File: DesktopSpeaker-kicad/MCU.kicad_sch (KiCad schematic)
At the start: 7 parts, among them J6 SWD, J7 SWD_TC2030, U3 STM32G031K8T6

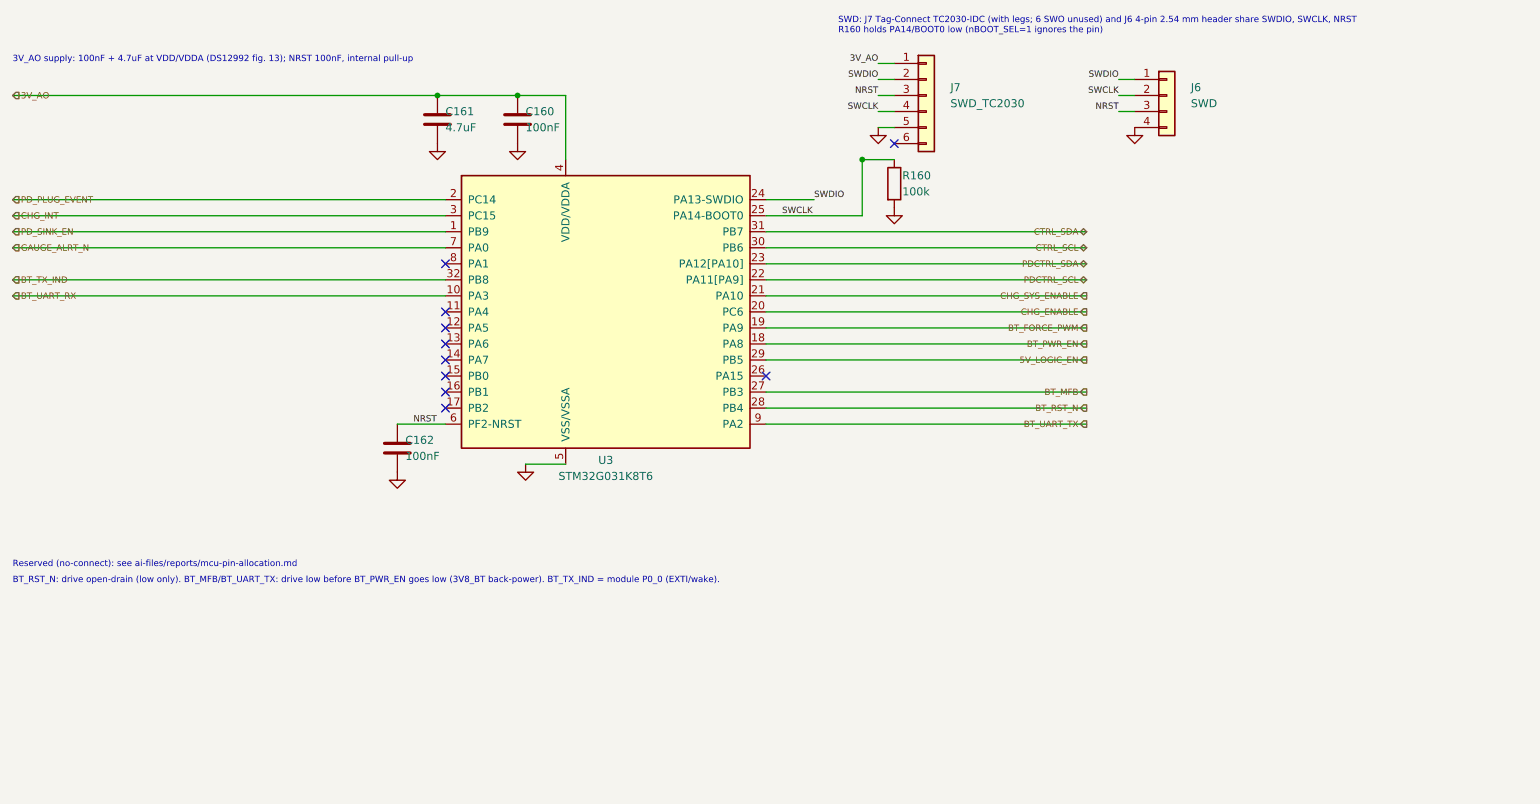
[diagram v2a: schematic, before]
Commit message: Swap MCU to STM32G071RBT6; full audio-chain pin allocation and QON sense
Co-Authored-By: Claude Sonnet 5.5 <noreply@anthropic.com>
Claude-Session: https://claude.ai/code/session_01N5RHheWSjDFDPbKVD5YVeJ
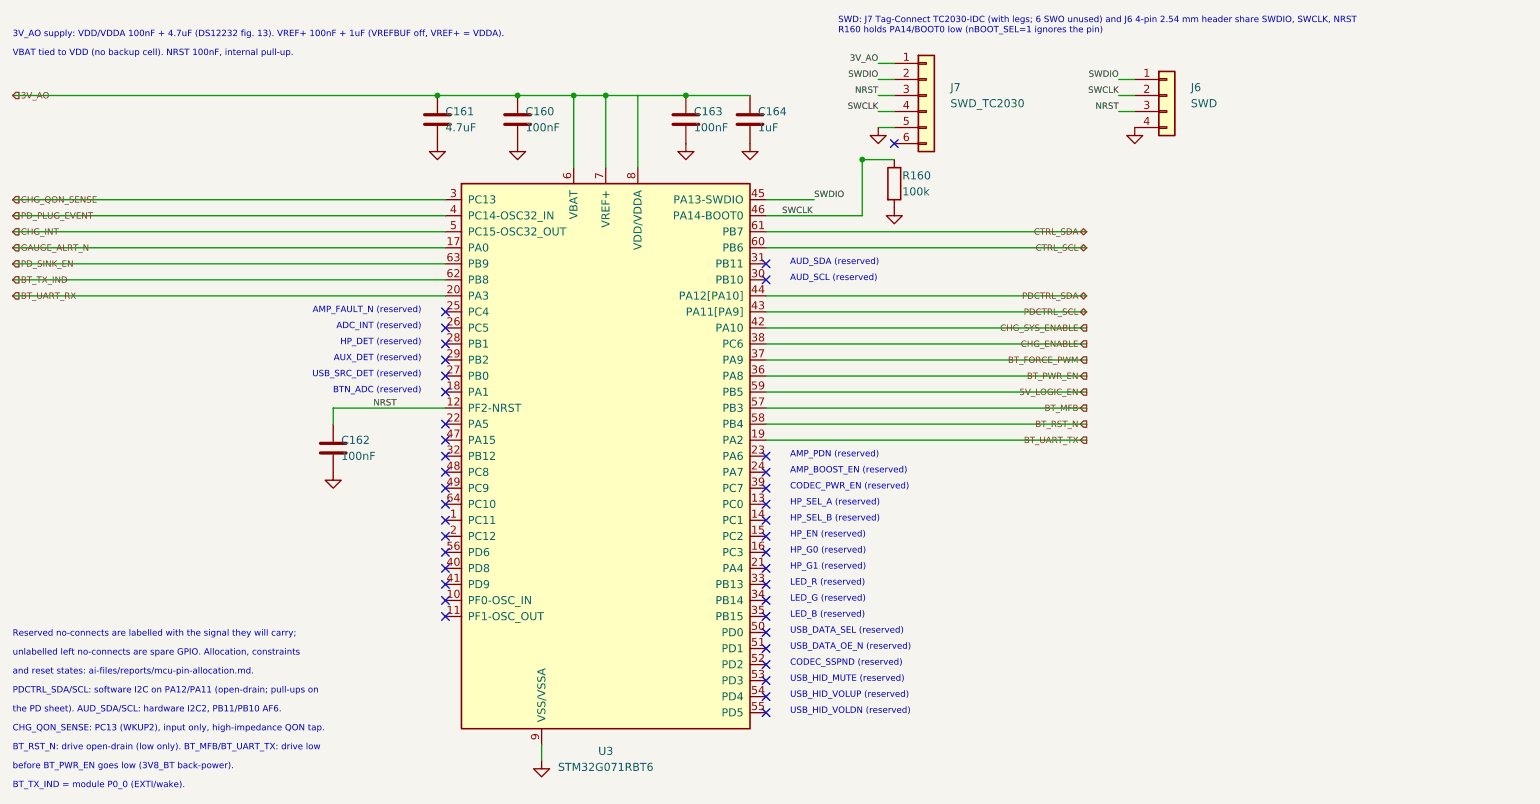
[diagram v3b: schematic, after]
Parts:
- added C163: 100nF, DesktopSpeaker:PD_C_0603, symbol PD_C:PD_C
- added C164: 1uF, DesktopSpeaker:PD_C_0603, symbol PD_C:PD_C
- U3: value STM32G031K8T6 -> STM32G071RBT6; footprint DesktopSpeaker:STM32G031K8T6 -> DesktopSpeaker:STM32G071RBT6; symbol STM32G031K8T6:STM32G031K8T6 -> STM32G071RBT6:STM32G071RBT6; LCSC Part C432203 -> C432213; MPN STM32G031K8T6 -> STM32G071RBT6
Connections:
- net 3V_AO: now also U3.6 (VBAT), U3.7 (VREF+), U3.8 (VDD/VDDA), C163.1, C164.1; no longer U3.4 (VDD/VDDA)
- net 5V_LOGIC_EN: now also U3.59 (PB5); no longer U3.29 (PB5)
- net BT_FORCE_PWM: now also U3.37 (PA9); no longer U3.19 (PA9)
- net BT_MFB: now also U3.57 (PB3); no longer U3.27 (PB3)
- net BT_PWR_EN: now also U3.36 (PA8); no longer U3.18 (PA8)
- net BT_RST_N: now also U3.58 (PB4); no longer U3.28 (PB4)
- net BT_TX_IND: now also U3.62 (PB8); no longer U3.32 (PB8)
- net BT_UART_RX: now also U3.20 (PA3); no longer U3.10 (PA3)
- net BT_UART_TX: now also U3.19 (PA2); no longer U3.9 (PA2)
- net CHG_ENABLE: now also U3.38 (PC6); no longer U3.20 (PC6)
- net CHG_INT: now also U3.5 (PC15-OSC32_OUT); no longer U3.3 (PC15)
- net CHG_SYS_ENABLE: now also U3.42 (PA10); no longer U3.21 (PA10)
- net CTRL_SCL: now also U3.60 (PB6); no longer U3.30 (PB6)
- net CTRL_SDA: now also U3.61 (PB7); no longer U3.31 (PB7)
- net GAUGE_ALRT_N: now also U3.17 (PA0); no longer U3.7 (PA0)
- net GND: now also U3.9 (VSS/VSSA), C163.2, C164.2; no longer U3.5 (VSS/VSSA)
- net NRST: now also U3.12 (PF2-NRST); no longer U3.6 (PF2-NRST)
- net PDCTRL_SCL: now also U3.43 (PA11[PA9]); no longer U3.22 (PA11[PA9])
- net PDCTRL_SDA: now also U3.44 (PA12[PA10]); no longer U3.23 (PA12[PA10])
- net PD_PLUG_EVENT: now also U3.4 (PC14-OSC32_IN); no longer U3.2 (PC14)
- net PD_SINK_EN: now also U3.63 (PB9); no longer U3.1 (PB9)
- net SWCLK: now also U3.46 (PA14-BOOT0); no longer U3.25 (PA14-BOOT0)
- net SWDIO: now also U3.45 (PA13-SWDIO); no longer U3.24 (PA13-SWDIO)
- new net CHG_QON_SENSE: U3.3 (PC13)
- no-connect marks 10 -> 39
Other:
- note added: "3V_AO supply: VDD/VDDA 100nF + 4.7uF (DS12232 fig. 13). VREF+ 100nF + 1uF (VREFBUF off, VREF+ = VDDA)."
- note added: "ADC_INT (reserved)"
- note added: "AMP_BOOST_EN (reserved)"
- note added: "AMP_FAULT_N (reserved)"
- note added: "AMP_PDN (reserved)"
- note added: "AUD_SCL (reserved)"
- note added: "AUD_SDA (reserved)"
- note added: "AUX_DET (reserved)"
- note added: "BTN_ADC (reserved)"
- note added: "BT_RST_N: drive open-drain (low only). BT_MFB/BT_UART_TX: drive low"
- note added: "BT_TX_IND = module P0_0 (EXTI/wake)."
- note added: "CHG_QON_SENSE: PC13 (WKUP2), input only, high-impedance QON tap."
- note added: "CODEC_PWR_EN (reserved)"
- note added: "CODEC_SSPND (reserved)"
- note added: "HP_DET (reserved)"
- note added: "HP_EN (reserved)"
- note added: "HP_G0 (reserved)"
- note added: "HP_G1 (reserved)"
- note added: "HP_SEL_A (reserved)"
- note added: "HP_SEL_B (reserved)"
- note added: "LED_B (reserved)"
- note added: "LED_G (reserved)"
- note added: "LED_R (reserved)"
- note added: "PDCTRL_SDA/SCL: software I2C on PA12/PA11 (open-drain; pull-ups on"
- note added: "Reserved no-connects are labelled with the signal they will carry;"
- note added: "USB_DATA_OE_N (reserved)"
- note added: "USB_DATA_SEL (reserved)"
- note added: "USB_HID_MUTE (reserved)"
- note added: "USB_HID_VOLDN (reserved)"
- note added: "USB_HID_VOLUP (reserved)"
- note added: "USB_SRC_DET (reserved)"
- note added: "VBAT tied to VDD (no backup cell). NRST 100nF, internal pull-up."
- note added: "and reset states: ai-files/reports/mcu-pin-allocation.md."
- note added: "before BT_PWR_EN goes low (3V8_BT back-power)."
- note added: "the PD sheet). AUD_SDA/SCL: hardware I2C2, PB11/PB10 AF6."
- note added: "unlabelled left no-connects are spare GPIO. Allocation, constraints"
- note removed: "3V_AO supply: 100nF + 4.7uF at VDD/VDDA (DS12992 fig. 13); NRST 100nF, internal pull-up"
- note removed: "BT_RST_N: drive open-drain (low only). BT_MFB/BT_UART_TX: drive low before BT_PWR_EN goes low (3V8_BT back-power). BT_TX_IND = module P0_0 (EXTI/wake)."
- note removed: "Reserved (no-connect): see ai-files/reports/mcu-pin-allocation.md"
- moved on the sheet: C162

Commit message: Capture Source_Select_ADC sheet (PCM1862, 3V3_AUDIO LDO, codec load switch)
Co-Authored-By: Claude Sonnet 5.5 <noreply@anthropic.com>
Claude-Session: https://claude.ai/code/session_01N5RHheWSjDFDPbKVD5YVeJ
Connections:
- net ADC_INT: now reaches U3.26 (PC5)
- net AUD_SCL: now reaches U3.30 (PB10)
- net AUD_SDA: now reaches U3.31 (PB11)
- net CODEC_PWR_EN: now reaches U3.39 (PC7)
- no-connect marks 39 -> 35
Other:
- note removed: "ADC_INT (reserved)"
- note removed: "AUD_SCL (reserved)"
- note removed: "AUD_SDA (reserved)"
- note removed: "CODEC_PWR_EN (reserved)"
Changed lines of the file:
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@@
 (no_connect (at 114.3 100.33))
 (text "AMP_FAULT_N (reserved)" (at 110.49 100.73 0) (effects (font (size 1 1)) (justify right bottom)))
-(no_connect (at 114.3 102.87))
-(text "ADC_INT (reserved)" (at 110.49 103.27 0) (effects (font (size 1 1)) (justify right bottom)))
 (no_connect (at 114.3 105.41))
 (text "HP_DET (reserved)" (at 110.49 105.81 0) (effects (font (size 1 1)) (justify right bottom)))
@@
 (wire (pts (xy 165.1 90.17) (xy 215.9 90.17)) (stroke (width 0) (type default)))
 (hierarchical_label "CTRL_SCL" (shape bidirectional) (at 215.9 90.17 0) (effects (font (size 1.0 1.0)) (justify right bottom)))
-(no_connect (at 165.1 92.71))
-(text "AUD_SDA (reserved)" (at 168.91 93.11 0) (effects (font (size 1 1)) (justify left bottom)))
-(no_connect (at 165.1 95.25))
-(text "AUD_SCL (reserved)" (at 168.91 95.65 0) (effects (font (size 1 1)) (justify left bottom)))
 (wire (pts (xy 165.1 97.79) (xy 215.9 97.79)) (stroke (width 0) (type default)))
 (hierarchical_label "PDCTRL_SDA" (shape bidirectional) (at 215.9 97.79 0) (effects (font (size 1.0 1.0)) (justify right bottom)))
@@
 (no_connect (at 165.1 125.73))
 (text "AMP_BOOST_EN (reserved)" (at 168.91 126.13 0) (effects (font (size 1 1)) (justify left bottom)))
-(no_connect (at 165.1 128.27))
-(text "CODEC_PWR_EN (reserved)" (at 168.91 128.67 0) (effects (font (size 1 1)) (justify left bottom)))
 (no_connect (at 165.1 130.81))
 (text "HP_SEL_A (reserved)" (at 168.91 131.21 0) (effects (font (size 1 1)) (justify left bottom)))
@@
 (text "before BT_PWR_EN goes low (3V8_BT back-power)." (at 45.72 173 0) (effects (font (size 1 1)) (justify left bottom)))
 (text "BT_TX_IND = module P0_0 (EXTI/wake)." (at 45.72 176 0) (effects (font (size 1 1)) (justify left bottom)))
+(wire (pts (xy 165.1 92.71) (xy 215.9 92.71)) (stroke (width 0) (type default)))
+(hierarchical_label "AUD_SDA" (shape bidirectional) (at 215.9 92.71 0) (effects (font (size 1.0 1.0)) (justify right bottom)))
+(wire (pts (xy 165.1 95.25) (xy 215.9 95.25)) (stroke (width 0) (type default)))
+(hierarchical_label "AUD_SCL" (shape bidirectional) (at 215.9 95.25 0) (effects (font (size 1.0 1.0)) (justify right bottom)))
+(wire (pts (xy 165.1 128.27) (xy 215.9 128.27)) (stroke (width 0) (type default)))
+(hierarchical_label "CODEC_PWR_EN" (shape output) (at 215.9 128.27 0) (effects (font (size 1.0 1.0)) (justify right bottom)))
+(wire (pts (xy 45.72 102.87) (xy 114.3 102.87)) (stroke (width 0) (type default)))
+(hierarchical_label "ADC_INT" (shape input) (at 45.72 102.87 0) (effects (font (size 1.0 1.0)) (justify left bottom)))
 )

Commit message: Capture Headphone_Aux sheet (TS5A23157 mux, TPA6132A2, jacks) and wire MCU headphone signals
Co-Authored-By: Claude Sonnet 5.5 <noreply@anthropic.com>
Claude-Session: https://claude.ai/code/session_01N5RHheWSjDFDPbKVD5YVeJ
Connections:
- net HP_SEL_A: now reaches U3.13 (PC0)
- net HP_SEL_B: now reaches U3.14 (PC1)
- net HP_EN: now reaches U3.15 (PC2)
- net HP_G0: now reaches U3.16 (PC3)
- net HP_G1: now reaches U3.21 (PA4)
- net HP_DET: now reaches U3.28 (PB1)
- net AUX_DET: now reaches U3.29 (PB2)
- no-connect marks 35 -> 28
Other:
- note removed: "AUX_DET (reserved)"
- note removed: "HP_DET (reserved)"
- note removed: "HP_EN (reserved)"
- note removed: "HP_G0 (reserved)"
- note removed: "HP_G1 (reserved)"
- note removed: "HP_SEL_A (reserved)"
- note removed: "HP_SEL_B (reserved)"
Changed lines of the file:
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@@
 (no_connect (at 114.3 100.33))
 (text "AMP_FAULT_N (reserved)" (at 110.49 100.73 0) (effects (font (size 1 1)) (justify right bottom)))
-(no_connect (at 114.3 105.41))
-(text "HP_DET (reserved)" (at 110.49 105.81 0) (effects (font (size 1 1)) (justify right bottom)))
-(no_connect (at 114.3 107.95))
-(text "AUX_DET (reserved)" (at 110.49 108.35 0) (effects (font (size 1 1)) (justify right bottom)))
 (no_connect (at 114.3 110.49))
 (text "USB_SRC_DET (reserved)" (at 110.49 110.89 0) (effects (font (size 1 1)) (justify right bottom)))
@@
 (no_connect (at 165.1 125.73))
 (text "AMP_BOOST_EN (reserved)" (at 168.91 126.13 0) (effects (font (size 1 1)) (justify left bottom)))
-(no_connect (at 165.1 130.81))
-(text "HP_SEL_A (reserved)" (at 168.91 131.21 0) (effects (font (size 1 1)) (justify left bottom)))
-(no_connect (at 165.1 133.35))
-(text "HP_SEL_B (reserved)" (at 168.91 133.75 0) (effects (font (size 1 1)) (justify left bottom)))
-(no_connect (at 165.1 135.89))
-(text "HP_EN (reserved)" (at 168.91 136.29 0) (effects (font (size 1 1)) (justify left bottom)))
-(no_connect (at 165.1 138.43))
-(text "HP_G0 (reserved)" (at 168.91 138.83 0) (effects (font (size 1 1)) (justify left bottom)))
-(no_connect (at 165.1 140.97))
-(text "HP_G1 (reserved)" (at 168.91 141.37 0) (effects (font (size 1 1)) (justify left bottom)))
 (no_connect (at 165.1 143.51))
 (text "LED_R (reserved)" (at 168.91 143.91 0) (effects (font (size 1 1)) (justify left bottom)))
@@
 (wire (pts (xy 45.72 102.87) (xy 114.3 102.87)) (stroke (width 0) (type default)))
 (hierarchical_label "ADC_INT" (shape input) (at 45.72 102.87 0) (effects (font (size 1.0 1.0)) (justify left bottom)))
+(wire (pts (xy 165.1 130.81) (xy 215.9 130.81)) (stroke (width 0) (type default)))
+(hierarchical_label "HP_SEL_A" (shape output) (at 215.9 130.81 0) (effects (font (size 1.0 1.0)) (justify right bottom)))
+(wire (pts (xy 165.1 133.35) (xy 215.9 133.35)) (stroke (width 0) (type default)))
+(hierarchical_label "HP_SEL_B" (shape output) (at 215.9 133.35 0) (effects (font (size 1.0 1.0)) (justify right bottom)))
+(wire (pts (xy 165.1 135.89) (xy 215.9 135.89)) (stroke (width 0) (type default)))
+(hierarchical_label "HP_EN" (shape output) (at 215.9 135.89 0) (effects (font (size 1.0 1.0)) (justify right bottom)))
+(wire (pts (xy 165.1 138.43) (xy 215.9 138.43)) (stroke (width 0) (type default)))
+(hierarchical_label "HP_G0" (shape output) (at 215.9 138.43 0) (effects (font (size 1.0 1.0)) (justify right bottom)))
+(wire (pts (xy 165.1 140.97) (xy 215.9 140.97)) (stroke (width 0) (type default)))
+(hierarchical_label "HP_G1" (shape output) (at 215.9 140.97 0) (effects (font (size 1.0 1.0)) (justify right bottom)))
+(wire (pts (xy 45.72 105.41) (xy 114.3 105.41)) (stroke (width 0) (type default)))
+(hierarchical_label "HP_DET" (shape input) (at 45.72 105.41 0) (effects (font (size 1.0 1.0)) (justify left bottom)))
+(wire (pts (xy 45.72 107.95) (xy 114.3 107.95)) (stroke (width 0) (type default)))
+(hierarchical_label "AUX_DET" (shape input) (at 45.72 107.95 0) (effects (font (size 1.0 1.0)) (justify left bottom)))
 )

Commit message: Capture Amplifiers sheet (TPS61088 boost, TAS5825M x2, speaker outputs); correct PBTL pairing
Co-Authored-By: Claude Sonnet 5.5 <noreply@anthropic.com>
Claude-Session: https://claude.ai/code/session_01N5RHheWSjDFDPbKVD5YVeJ
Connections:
- net AMP_PDN: now reaches U3.23 (PA6)
- net AMP_BOOST_EN: now reaches U3.24 (PA7)
- net AMP_FAULT_N: now reaches U3.25 (PC4)
- no-connect marks 28 -> 25
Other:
- note removed: "AMP_BOOST_EN (reserved)"
- note removed: "AMP_FAULT_N (reserved)"
- note removed: "AMP_PDN (reserved)"
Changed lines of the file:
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@@
 (wire (pts (xy 45.72 97.79) (xy 114.3 97.79)) (stroke (width 0) (type default)))
 (hierarchical_label "BT_UART_RX" (shape input) (at 45.72 97.79 0) (effects (font (size 1.0 1.0)) (justify left bottom)))
-(no_connect (at 114.3 100.33))
-(text "AMP_FAULT_N (reserved)" (at 110.49 100.73 0) (effects (font (size 1 1)) (justify right bottom)))
 (no_connect (at 114.3 110.49))
 (text "USB_SRC_DET (reserved)" (at 110.49 110.89 0) (effects (font (size 1 1)) (justify right bottom)))
@@
 (wire (pts (xy 165.1 120.65) (xy 215.9 120.65)) (stroke (width 0) (type default)))
 (hierarchical_label "BT_UART_TX" (shape output) (at 215.9 120.65 0) (effects (font (size 1.0 1.0)) (justify right bottom)))
-(no_connect (at 165.1 123.19))
-(text "AMP_PDN (reserved)" (at 168.91 123.59 0) (effects (font (size 1 1)) (justify left bottom)))
-(no_connect (at 165.1 125.73))
-(text "AMP_BOOST_EN (reserved)" (at 168.91 126.13 0) (effects (font (size 1 1)) (justify left bottom)))
 (no_connect (at 165.1 143.51))
 (text "LED_R (reserved)" (at 168.91 143.91 0) (effects (font (size 1 1)) (justify left bottom)))
@@
 (wire (pts (xy 45.72 107.95) (xy 114.3 107.95)) (stroke (width 0) (type default)))
 (hierarchical_label "AUX_DET" (shape input) (at 45.72 107.95 0) (effects (font (size 1.0 1.0)) (justify left bottom)))
+(wire (pts (xy 165.1 123.19) (xy 215.9 123.19)) (stroke (width 0) (type default)))
+(hierarchical_label "AMP_PDN" (shape output) (at 215.9 123.19 0) (effects (font (size 1.0 1.0)) (justify right bottom)))
+(wire (pts (xy 165.1 125.73) (xy 215.9 125.73)) (stroke (width 0) (type default)))
+(hierarchical_label "AMP_BOOST_EN" (shape output) (at 215.9 125.73 0) (effects (font (size 1.0 1.0)) (justify right bottom)))
+(wire (pts (xy 45.72 100.33) (xy 114.3 100.33)) (stroke (width 0) (type default)))
+(hierarchical_label "AMP_FAULT_N" (shape input) (at 45.72 100.33 0) (effects (font (size 1.0 1.0)) (justify left bottom)))
 )

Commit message: Repackage passives to 0402/0805 hand-solder footprints; update BOM and flags
Co-Authored-By: Claude Sonnet 5.5 <noreply@anthropic.com>
Claude-Session: https://claude.ai/code/session_01N5RHheWSjDFDPbKVD5YVeJ
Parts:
- C160, C162, C163: footprint DesktopSpeaker:PD_C_0603 -> DesktopSpeaker:C_0402_1005Metric_Pad0.74x0.62mm_HandSolder; LCSC C1591 -> C77020; MPN CL10B104KB8NNNC -> GRM155R71H104KE14D; Manufacturer Samsung Electro-Mechanics -> Murata
- C161: footprint DesktopSpeaker:PD_C_0603 -> DesktopSpeaker:C_0805_2012Metric_Pad1.18x1.45mm_HandSolder; LCSC C19666 -> (none); MPN CL10A475KO8NNNC -> CL21A475KAQNNNE
- C164: footprint DesktopSpeaker:PD_C_0603 -> DesktopSpeaker:C_0402_1005Metric_Pad0.74x0.62mm_HandSolder; LCSC C15849 -> C29266; MPN CL10A105KB8NNNC -> CL05A105KO5NNNC
- R160: footprint DesktopSpeaker:PD_R_0603 -> DesktopSpeaker:R_0402_1005Metric_Pad0.72x0.64mm_HandSolder; LCSC C14675 -> C60491; MPN RC0603FR-07100KL -> RC0402FR-07100KL; Manufacturer YAGEO -> Yageo
